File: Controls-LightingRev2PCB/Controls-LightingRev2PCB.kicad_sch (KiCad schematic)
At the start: 22 parts, among them J1 Conn_01x04, J10 Conn_01x03, J6 Conn_01x02, J8 Conn_01x03, J9 PeripheralCANConnector, Q1 Si2319CDS, U1 SN65HVD230, U12 74AHCT125, U2 TLV9301xDCK, U3 TLV9301xDCK, U5 SiA462DJ

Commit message: cleaned up repo
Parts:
- removed J9: PeripheralCANConnector, UTSVT_Connectors:Molex_MicroFit3.0_1x4xP3.00mm_PolarizingPeg_Vertical, symbol utsvt-connectors:PeripheralCANConnector
- removed R6: 100, symbol Device:R_US
- removed U1: SN65HVD230, Package_SO:SOIC-8_3.9x4.9mm_P1.27mm, symbol Interface_CAN_LIN:SN65HVD230
- added J2: Conn_01x04, symbol Connector_Generic:Conn_01x04
- added U4: PeripheralSOM, UTSVT_Special:PeripheralSOM, symbol utsvt-misc:PeripheralSOM
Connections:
- net +24V: no longer U5.1 (D)
- net +3.3V: no longer J1.1 (Pin_1)
- net GND: now also J2.4 (Pin_4)
- net CAN_RX renamed CAN_L
- net CAN_L: now also J2.3 (Pin_3)
- net CAN_TX renamed CAN_H
- net CAN_H: now also J2.2 (Pin_2)
- new net 12V: J1.1 (Pin_1), J2.1 (Pin_1)

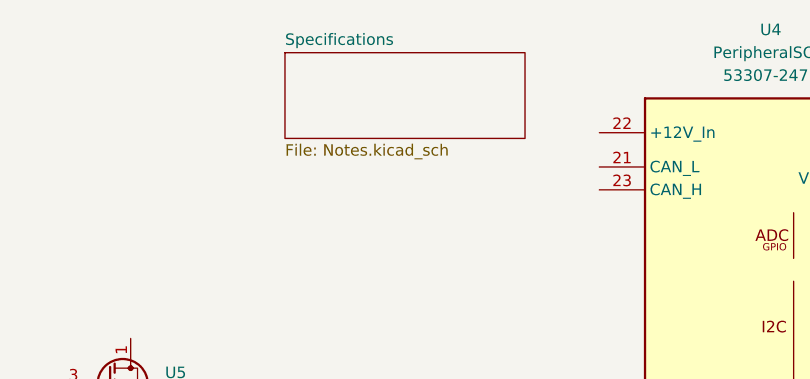
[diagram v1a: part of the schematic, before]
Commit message: Need 24V to 5V from PSOM PCB
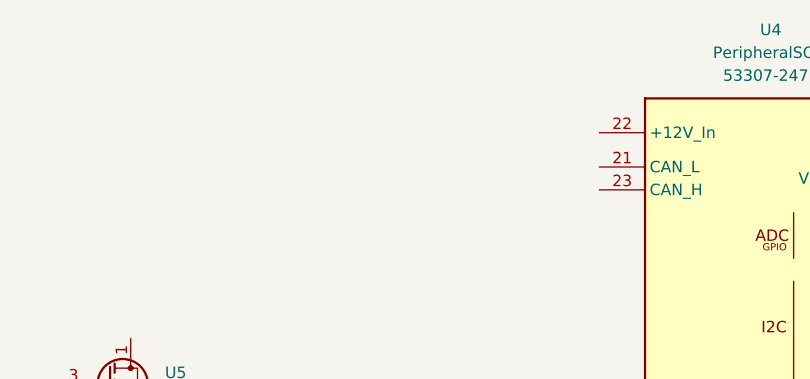
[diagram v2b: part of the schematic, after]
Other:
- removed sheet Specifications
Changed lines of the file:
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@@
-		)
-	)
-	(sheet
-		(at 255.905 17.78)
-		(size 26.67 9.525)
-		(exclude_from_sim no)
-		(in_bom yes)
-		(on_board yes)
-		(dnp no)
-		(fields_autoplaced yes)
-		(stroke
-			(width 0.1524)
-			(type solid)
-		)
-		(fill
-			(color 0 0 0 0.0000)
-		)
-		(property "Sheetname" "Specifications"
-			(at 255.905 17.0684 0)
-			(effects
-				(font
-					(size 1.27 1.27)
-				)
-				(justify left bottom)
-			)
-		)
-		(property "Sheetfile" "Notes.kicad_sch"
-			(at 255.905 27.8896 0)
-			(effects
-				(font
-					(size 1.27 1.27)
-				)
-				(justify left top)
-			)
-		)
-		(instances
-			(project "Controls-LightingRev2PCB"
-				(path "/4b4aadb4-8255-4dd1-afed-8a54e6d292d4"
-					(page "2")
-				)
-			)
 		)
 	)
